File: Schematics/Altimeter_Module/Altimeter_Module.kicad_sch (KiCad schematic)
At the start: 106 parts, among them J1 Stack Male Edge Connector, J2 Main E-Match, J3 Drogue E-Match, J4 USB_C_Female_USB2_Small, J5 SWD_01x04_Pin, Q1 AO3400A, Q2 AO4406AL, Q3 AO3400A, Q4 AO3400A, Q5 AO4406AL, SW1 SW_STM_RESET, SW2 SW_STM_BOOT_MODE, U1 KX134-1211, U10 ACS70331EOLC, U12 AMS1117-3.3, U2 MS560702BA03-50, U3 W25Q128JVS, U4 LM66100DCKR, U5 LM66100DCKR, U6 STM32F103CBT6, U7 LM66100DCKR, U8 ISO1042BDWVR, U9 MPU-6050, Y1 X322516MMB4SI

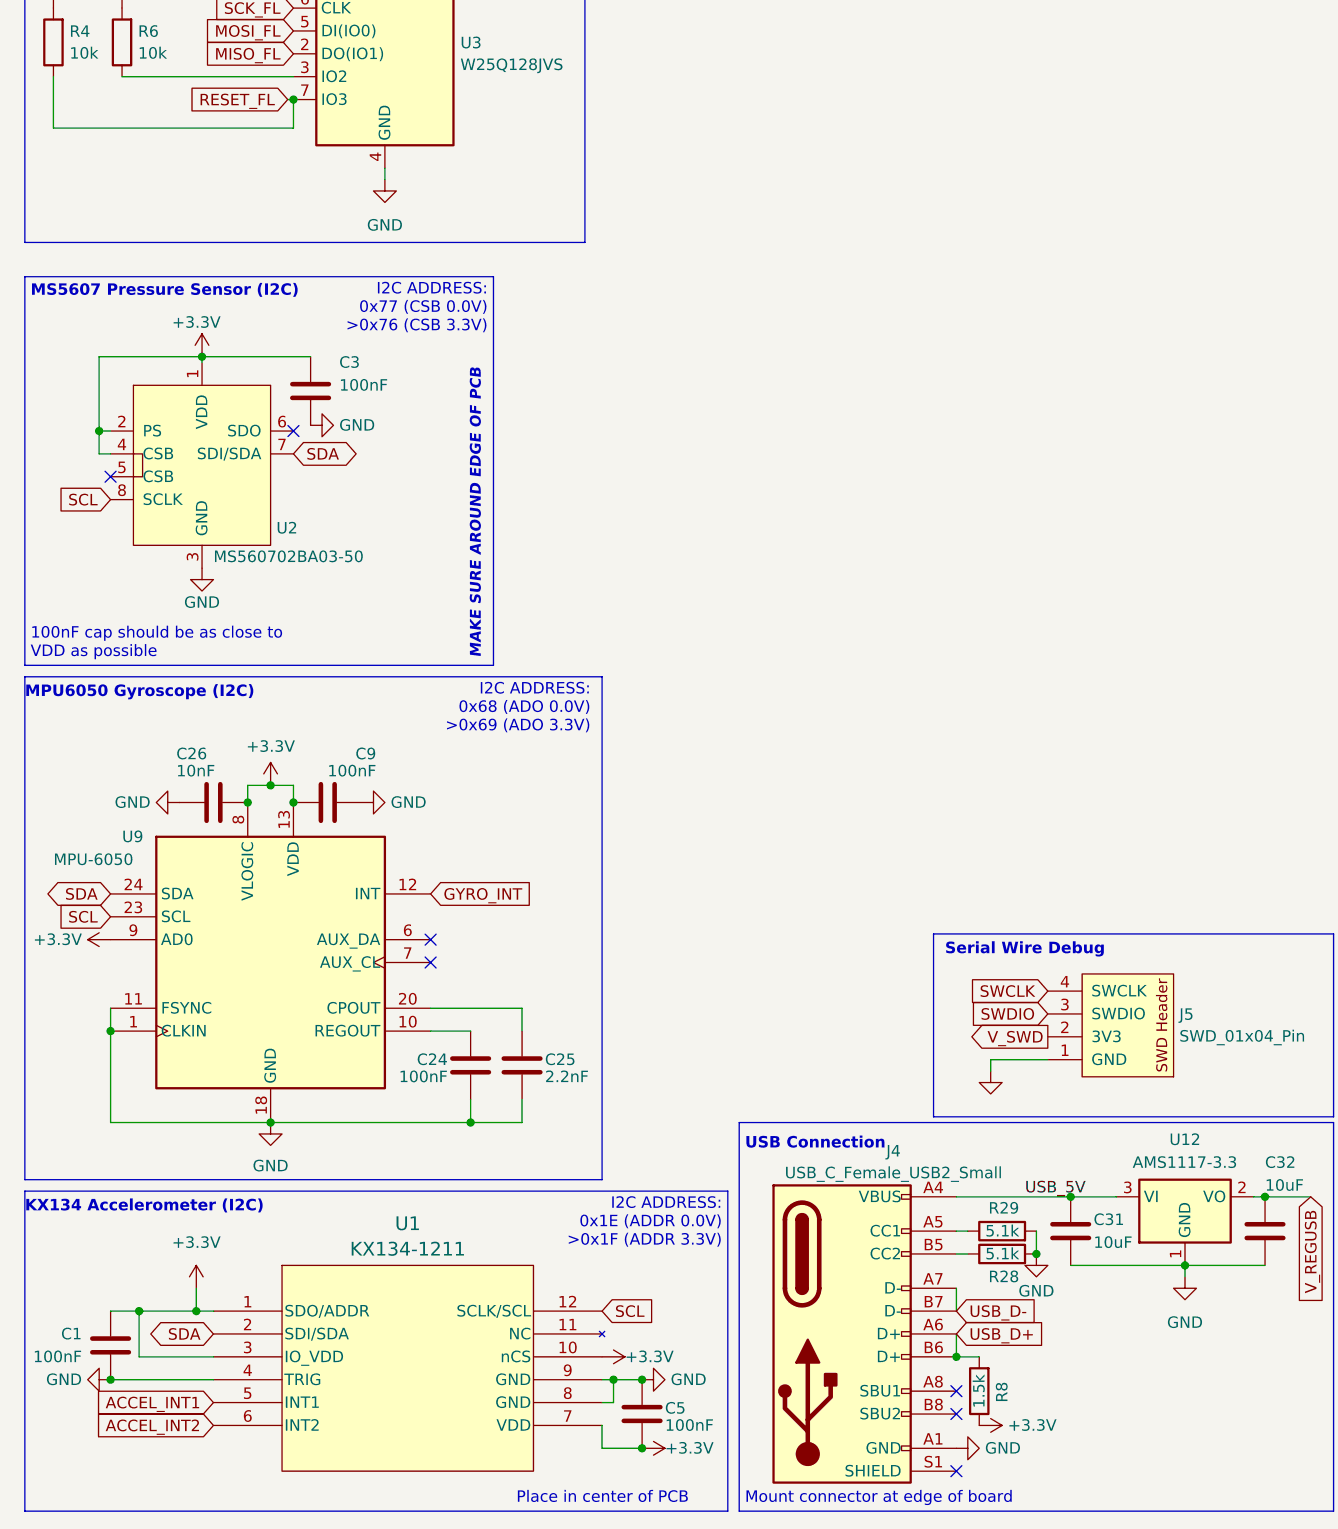
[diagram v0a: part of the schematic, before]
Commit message: Added note about Accelerometer change
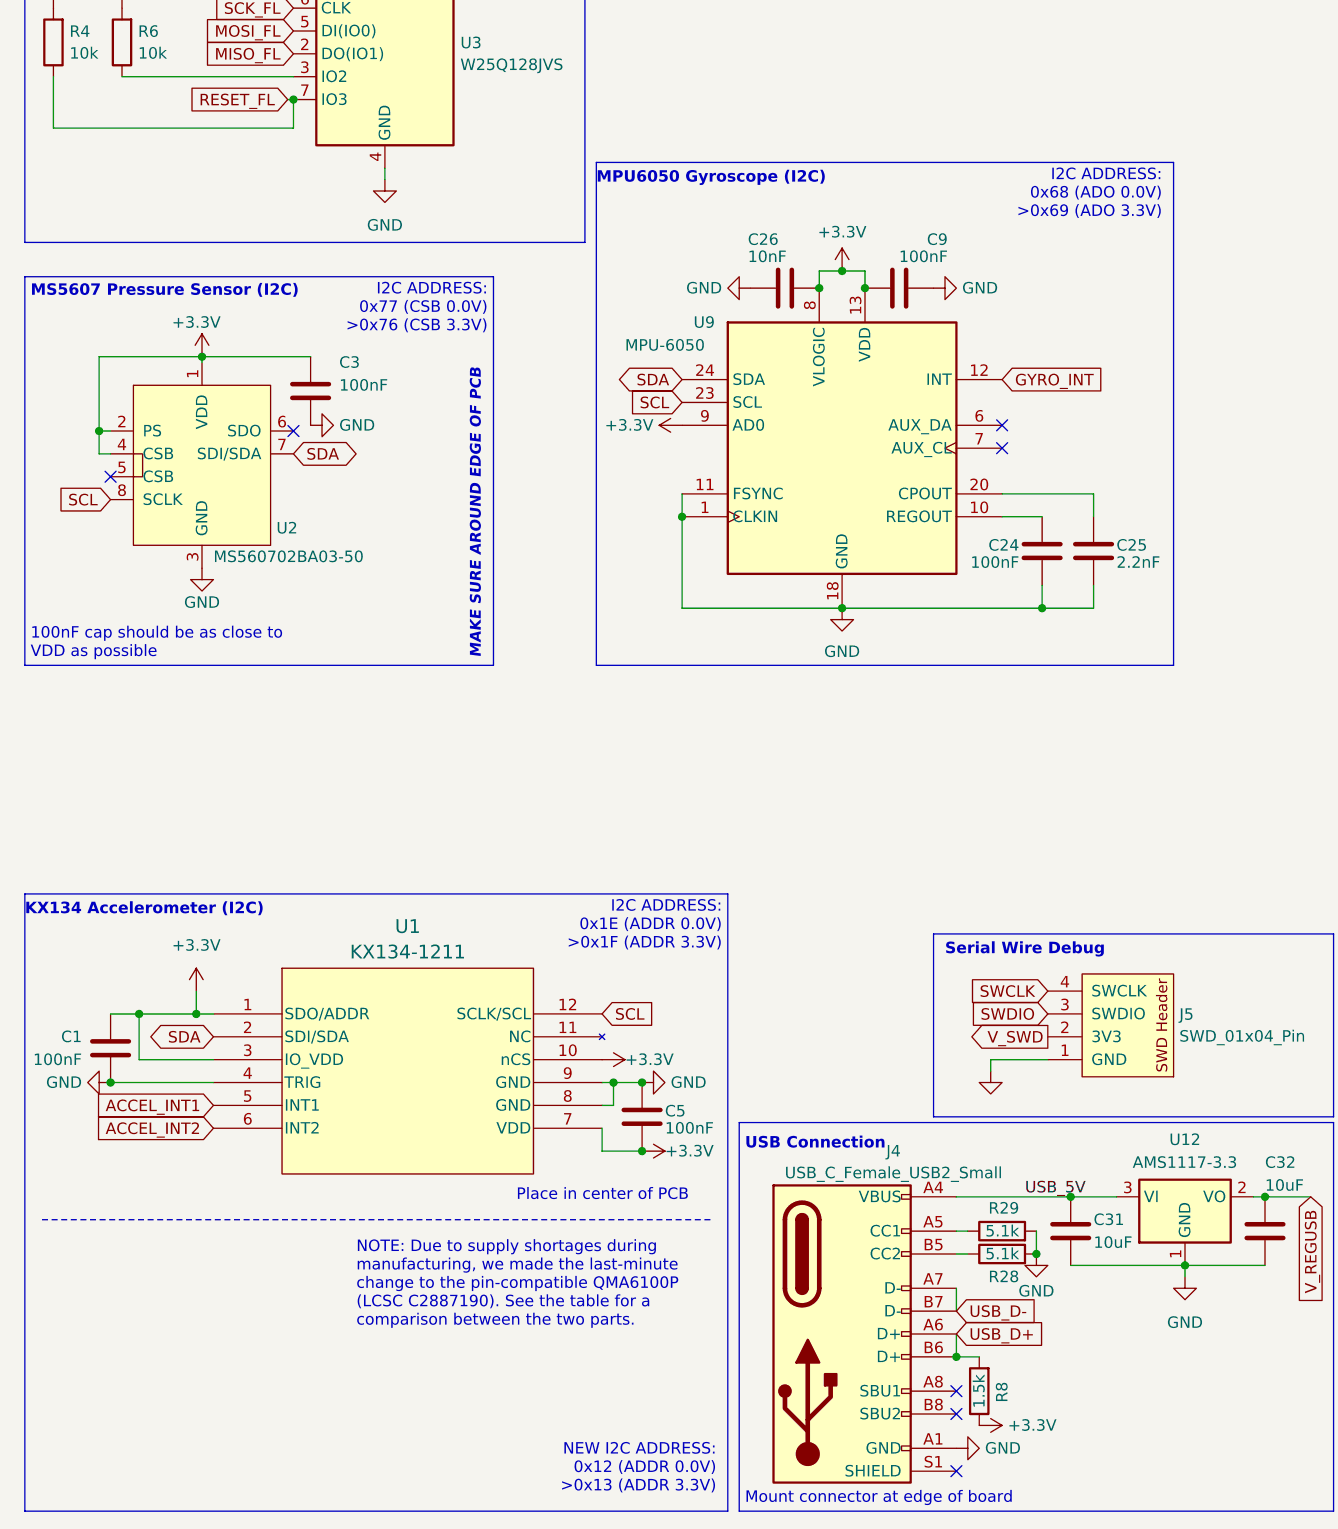
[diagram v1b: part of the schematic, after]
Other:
- note added: "NEW I2C ADDRESS: 0x12 (ADDR 0.0V) >0x13 (ADDR 3.3V)"
- note added: "NOTE: Due to supply shortages during manufacturing, we made the last-minute change to the pin-compatible QMA6100P (LCSC C2887190). See the table for a comparison between the two parts."
- moved on the sheet: C1, C24, C25, C26, C5, C9, U1, U9

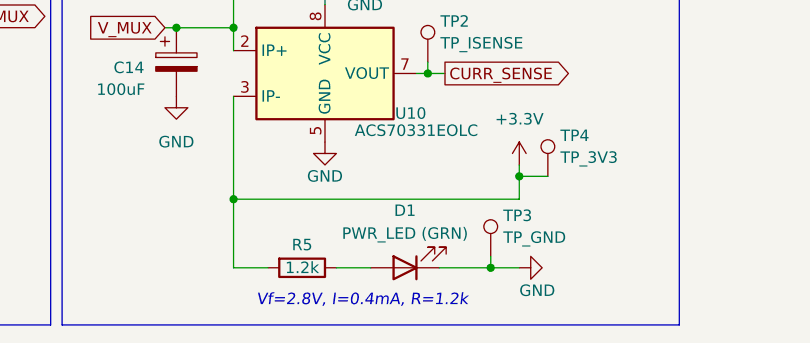
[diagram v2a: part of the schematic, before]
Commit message: Reduced power LED brightness (3.3k resistor)
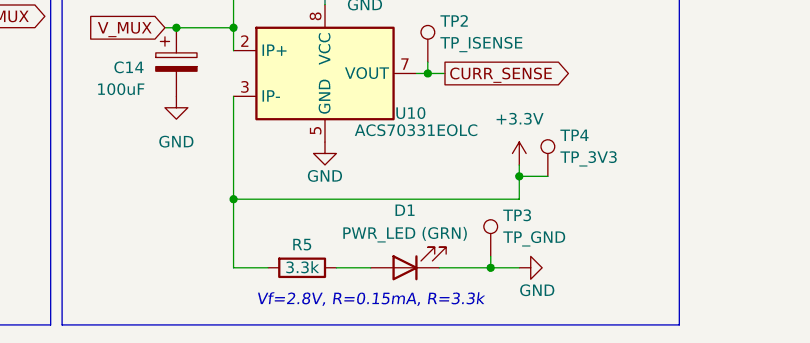
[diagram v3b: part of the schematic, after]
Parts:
- R5: value 1.2k -> 3.3k; LCSC C22765 -> C22978
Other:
- note added: "Vf=2.8V, R=0.15mA, R=3.3k"
- note removed: "Vf=2.8V, I=0.4mA, R=1.2k"
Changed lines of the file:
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@@
     (effects (font (size 1.27 1.27) (thickness 0.254) bold) (justify left bottom))
   )
-  (text "Vf=2.8V, I=0.4mA, R=1.2k" (at 263.525 264.16 0)
+  (text "Vf=2.8V, R=0.15mA, R=3.3k" (at 263.525 264.16 0)
     (effects (font (size 1.27 1.27) italic) (justify left bottom))
   )
@@
       (effects (font (size 1.27 1.27)))
     )
-    (property "Value" "1.2k" (at 268.605 259.715 90)
+    (property "Value" "3.3k" (at 268.605 259.715 90)
       (effects (font (size 1.27 1.27)))
     )
@@
       (effects (font (size 1.27 1.27)) hide)
     )
-    (property "LCSC" "C22765" (at 268.605 259.715 0)
-      (effects (font (size 1.27 1.27)) hide)
-    )
+    (property "LCSC" "C22978" (at 268.605 259.715 0)
+      (effects (font (size 1.27 1.27)) hide)
+    )

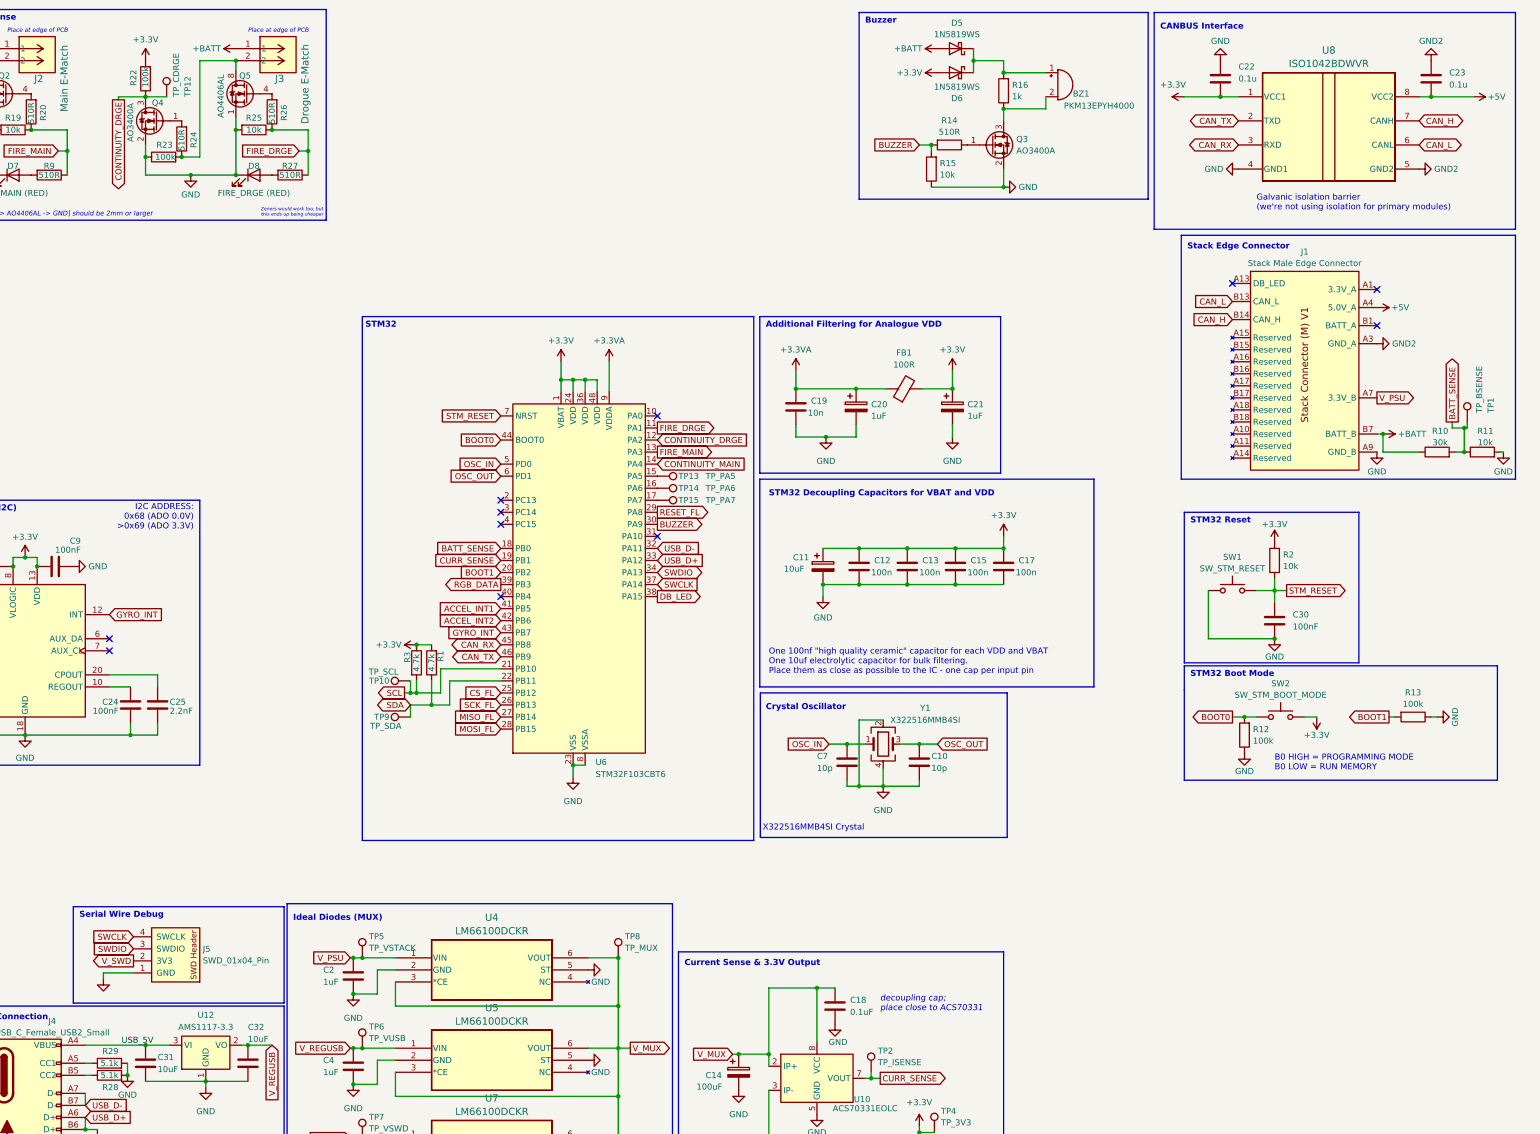
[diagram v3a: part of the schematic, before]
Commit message: Added CP2102 USB bridge
Also bumped version up to V2.0 now that significant hardware changes (e.g. pinout changes) have been made. This breaks firmware backwards compatibility, and thus warrants a major version bump.
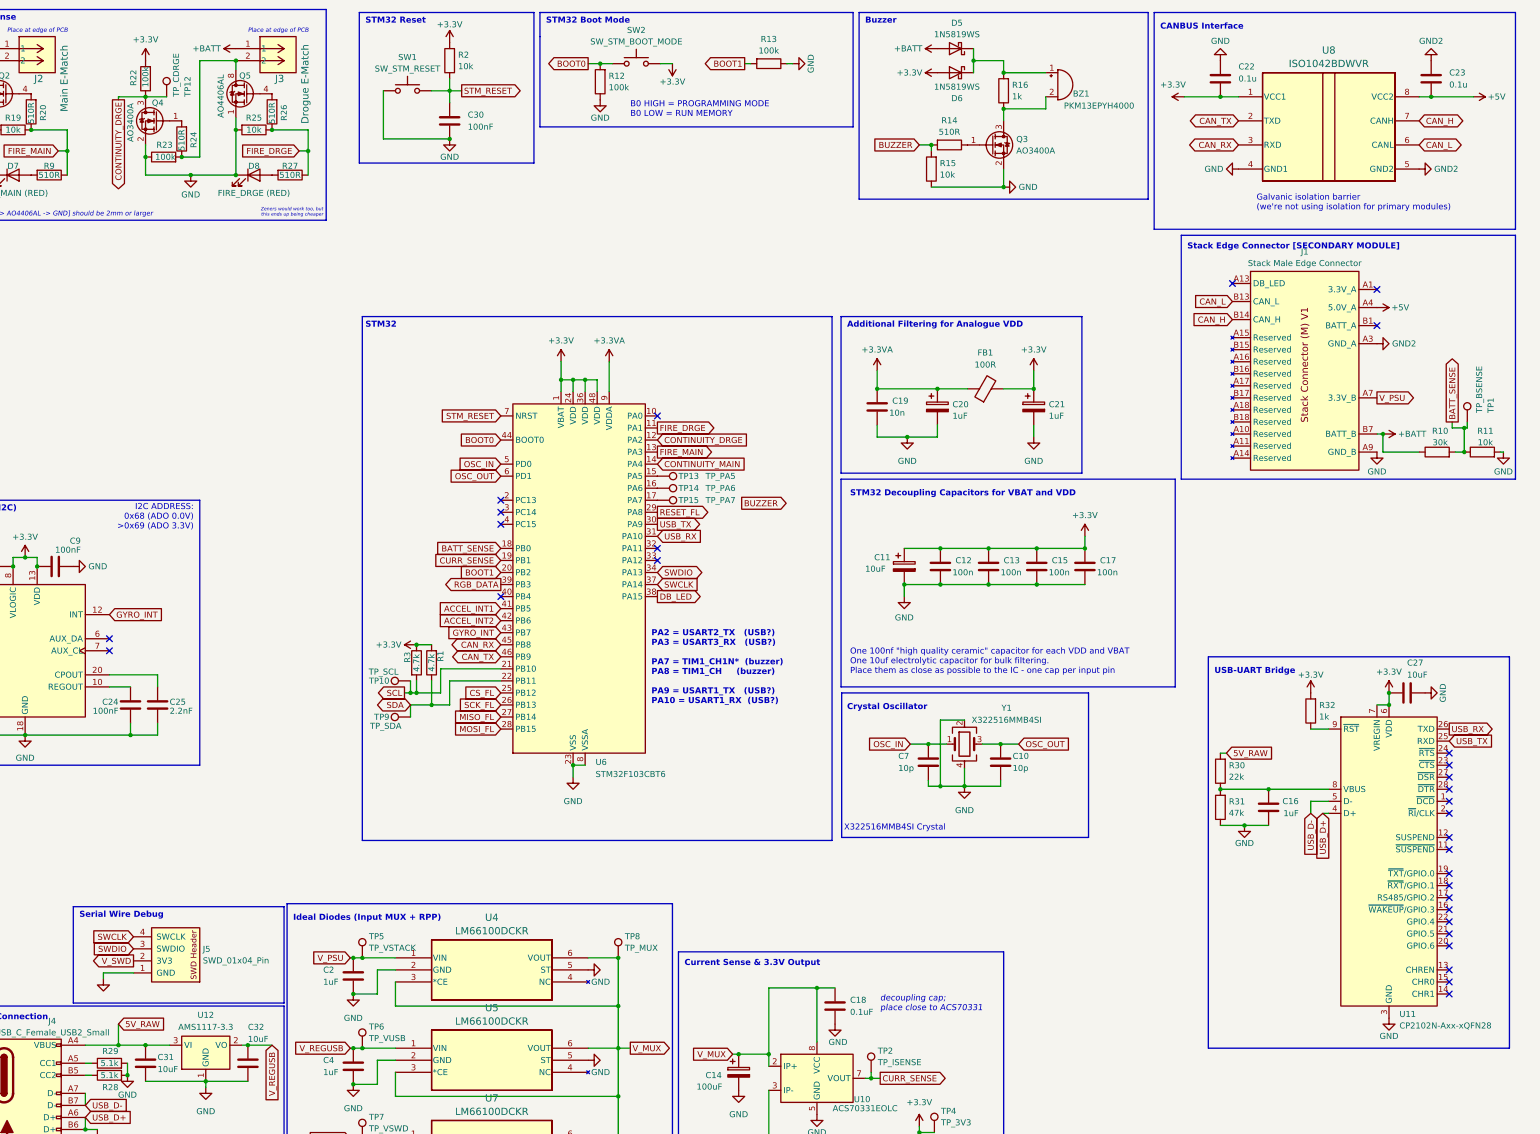
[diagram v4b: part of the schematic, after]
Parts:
- added C16: 1uF, Capacitor_SMD:C_0603_1608Metric, symbol Device:C
- added C27: 10uF, Capacitor_SMD:C_0603_1608Metric, symbol Device:C
- added R30: 22k, Resistor_SMD:R_0603_1608Metric, symbol Device:R
- added R31: 47k, Resistor_SMD:R_0603_1608Metric, symbol Device:R
- added R32: 1k, Resistor_SMD:R_0603_1608Metric, symbol Device:R
- added U11: CP2102N-Axx-xQFN28, Package_DFN_QFN:QFN-28-1EP_5x5mm_P0.5mm_EP3.35x3.35mm, symbol Interface_USB:CP2102N-Axx-xQFN28
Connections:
- net +3.3V: now also C27.2, R32.2, U11.6 (VDD), U11.7 (VREGIN)
- net BUZZER: no longer U6.30 (PA9)
- net GND: now also C16.1, C27.1, R31.1, U11.29 (GND), U11.3 (GND)
- net USB_D+: now also U11.4 (D+); no longer U6.33 (PA12)
- net USB_D-: now also U11.5 (D-); no longer U6.32 (PA11)
- net USB_RX: now reaches U6.31 (PA10)
- net USB_RX: now also U11.26 (TXD)
- net USB_5V renamed 5V_RAW
- net 5V_RAW: now also R30.2
- new net: C16.2, R30.1, R31.2, U11.8 (VBUS)
- new net: R32.1, U11.9 (~{RST})
- new net USB_TX: U11.25 (RXD), U6.30 (PA9)
- no-connect marks 17 -> 36
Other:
- note added: "Ideal Diodes (Input MUX + RPP)"
- note added: "PA2 = USART2_TX (USB?) PA3 = USART3_RX (USB?) PA7 = TIM1_CH1N* (buzzer) PA8 = TIM1_CH (buzzer) PA9 = USART1_TX (USB?) PA10 = USART1_RX (USB?)"
- note added: "Stack Edge Connector [SECONDARY MODULE]"
- note added: "USB-UART Bridge"
- note removed: "Ideal Diodes (MUX)"
- note removed: "Stack Edge Connector"
- moved on the sheet: C10, C11, C12, C13, C15, C17, C19, C20, C21, C30, C7, FB1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
